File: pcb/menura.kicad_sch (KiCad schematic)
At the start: 56 parts, among them SW1 SW_Push, SW10 SW_Push, SW11 SW_Push, SW12 SW_Push, SW13 SW_Push, SW14 SW_Push, SW15 SW_Push, SW16 SW_Push, SW17 SW_Push, SW18 SW_Push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

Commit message: bird silhouette logo
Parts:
- removed LOGO2: vik, quappo:Logo_vik-small, symbol Graphic:Logo_Open_Hardware_Small
- LOGO1: value menura -> menura_composite; footprint quappo:Logo_menura -> quappo:Logo_menura_composite
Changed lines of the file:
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@@
 			)
 		)
-		(property "Value" "menura"
+		(property "Value" "menura_composite"
 			(at 90.17 145.4149 0)
 			(effects
@@
 			)
 		)
-		(property "Footprint" "quappo:Logo_menura"
+		(property "Footprint" "quappo:Logo_menura_composite"
 			(at 83.82 144.78 0)
 			(effects
@@
 					(unit 1)
 				)
-			)
-		)
-	)
-	(symbol
-		(lib_id "Graphic:Logo_Open_Hardware_Small")
-		(at 109.22 144.78 0)
-		(unit 1)
-		(exclude_from_sim yes)
-		(in_bom no)
-		(on_board yes)
-		(dnp no)
-		(fields_autoplaced yes)
-		(property "Reference" "LOGO2"
-			(at 115.57 142.8749 0)
-			(effects
-				(font
-					(size 1.27 1.27)
-				)
-				(justify left)
-			)
-		)
-		(property "Value" "vik"
-			(at 115.57 145.4149 0)
-			(effects
-				(font
-					(size 1.27 1.27)
-				)
-				(justify left)
-			)
-		)
-		(property "Footprint" "quappo:Logo_vik-small"
-			(at 109.22 144.78 0)
-			(effects
-				(font
-					(size 1.27 1.27)
-				)
-				(hide yes)
-			)
-		)
-		(property "Datasheet" "~"
-			(at 109.22 144.78 0)
-			(effects
-				(font
-					(size 1.27 1.27)
-				)
-				(hide yes)
-			)
-		)
-		(property "Description" "Open Hardware logo, small"
-			(at 109.22 144.78 0)
-			(effects
-				(font
-					(size 1.27 1.27)
-				)
-				(hide yes)
-			)
-		)
-		(instances
-			(project "menura"
-				(path "/e9ea61dd-32b8-44c9-bab5-2f724da397cf"
-					(reference "LOGO2")
-					(unit 1)
-				)

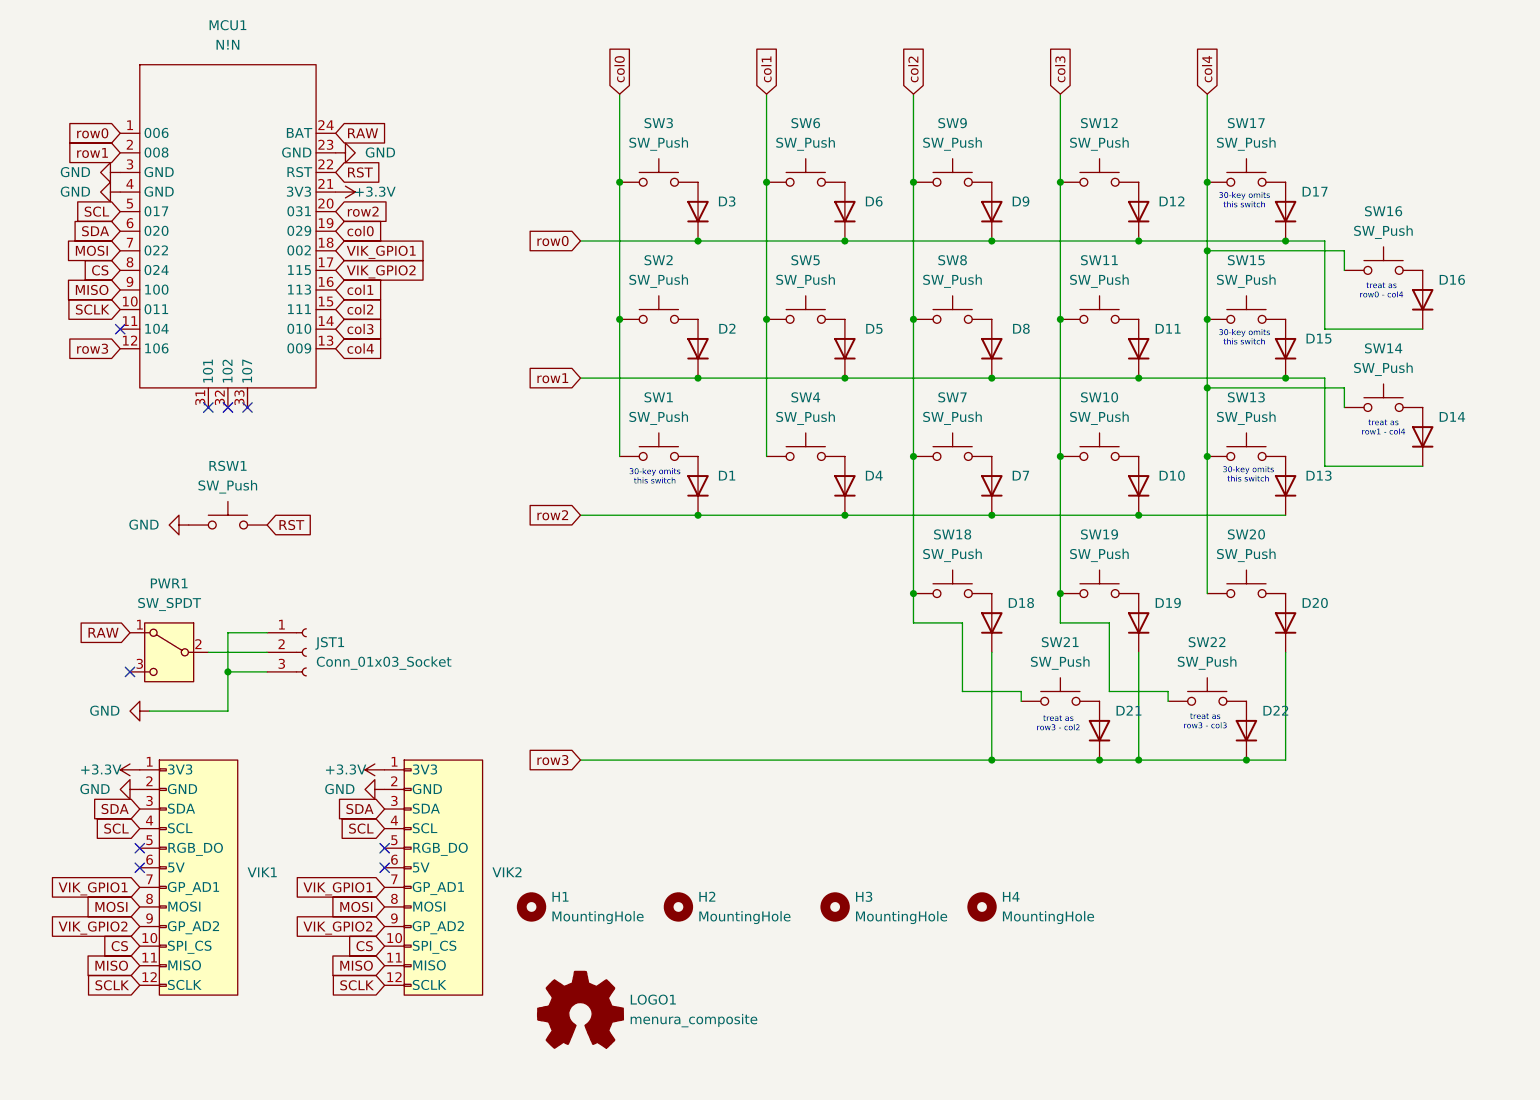
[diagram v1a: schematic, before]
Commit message: satisfy erc
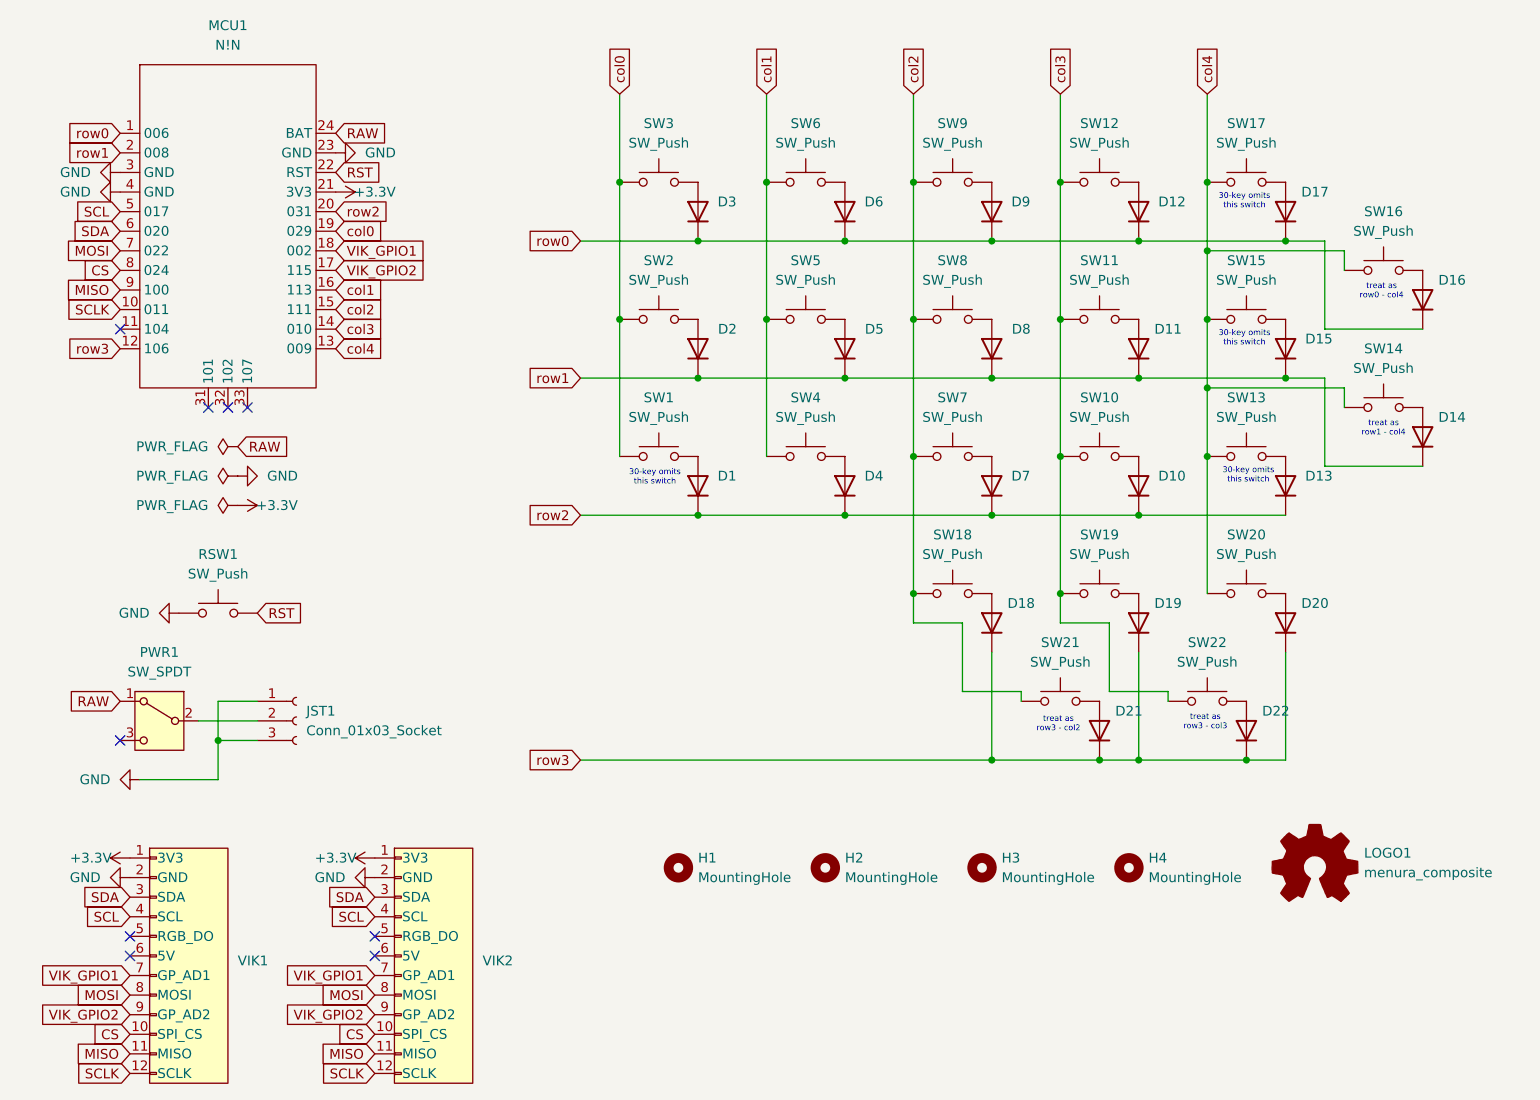
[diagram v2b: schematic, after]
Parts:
- VIK1, VIK2: symbol _quappo:vik-keyboard-connector -> quappo:vik-keyboard-connector
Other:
- moved on the sheet: H1, H2, H3, H4, JST1, LOGO1, PWR1, RSW1, VIK1, VIK2
